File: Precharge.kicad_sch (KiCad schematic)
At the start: 27 parts, among them J1 SDC_OUT, J2 TSAL, J3 BMS, J4 SDC_IN, J5 CONN_ACC, J6 CONN_INV, J7 CONN_TSAL, K1 G2RG-2A-X DC12, K2 G2RL-1-E

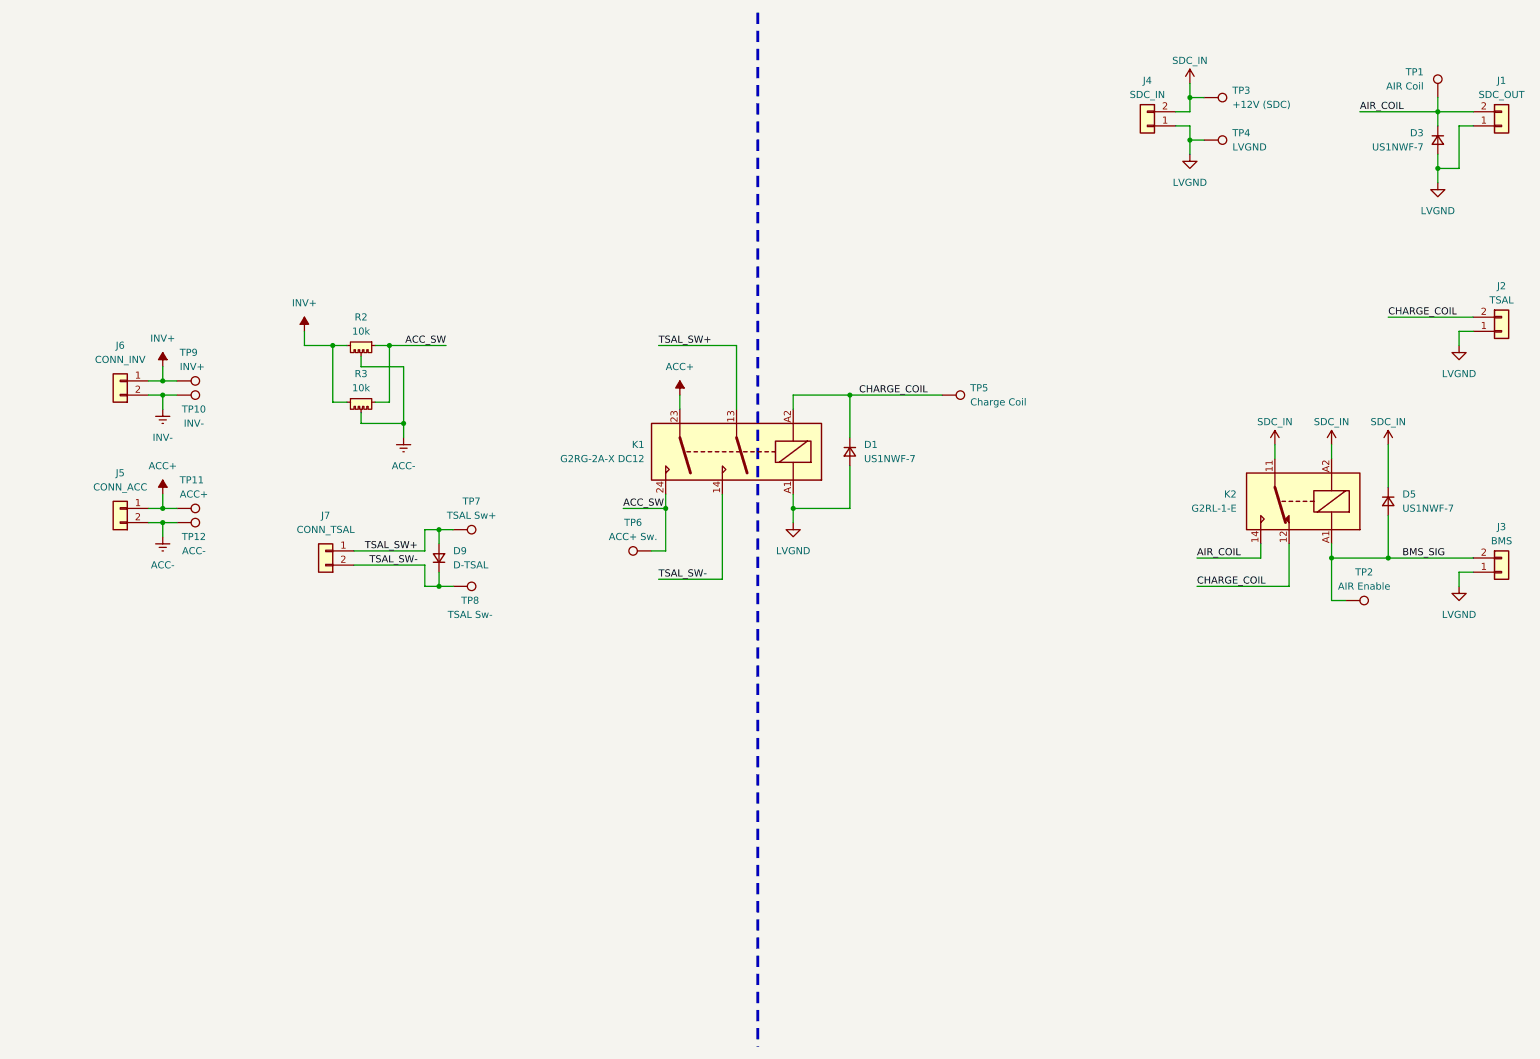
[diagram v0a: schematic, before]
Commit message: New schematic
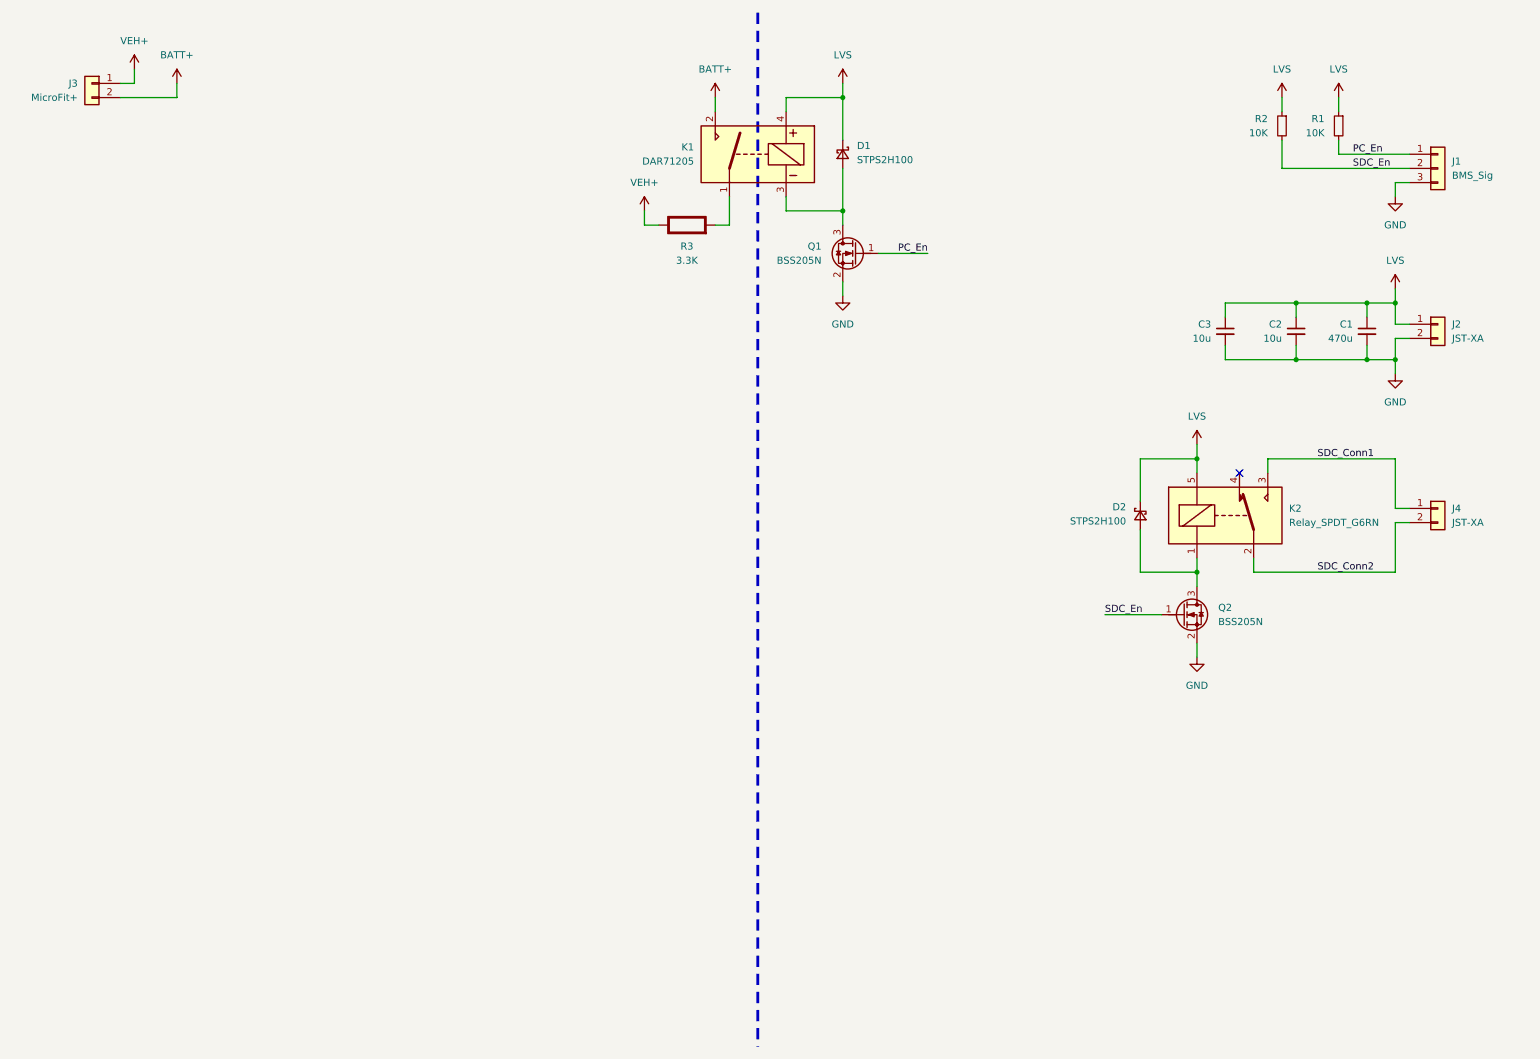
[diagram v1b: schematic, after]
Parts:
- removed D1, D3, D5: US1NWF-7, Diode_SMD:D_SOD-123F, symbol Device:D_Small
- removed D9: D-TSAL, Diode_SMD:D_SOD-123, symbol Device:D_Small
- removed J1: SDC_OUT, molexMiniFitJr:MFJ_2X1, symbol Connector_Generic:Conn_01x02
- removed J2: TSAL, molexMiniFitJr:MFJ_2X1, symbol Connector_Generic:Conn_01x02
- removed J3: BMS, molexMiniFitJr:MFJ_2X1, symbol Connector_Generic:Conn_01x02
- removed J4: SDC_IN, molexMiniFitJr:MFJ_2X1, symbol Connector_Generic:Conn_01x02
- removed J5: CONN_ACC, customFootprints:APP_ASMPR45-1X2-RK, symbol Connector_Generic:Conn_01x02
- removed J6: CONN_INV, customFootprints:APP_ASMPR45-1X2-RK, symbol Connector_Generic:Conn_01x02
- removed J7: CONN_TSAL, molexMiniFitJr:MFJ_2X1, symbol Connector_Generic:Conn_01x02
- removed K1: G2RG-2A-X DC12, Relay_THT:Relay_DPST_Omron_G2RL-2A, symbol Relay:G2RL-2A
- removed K2: G2RL-1-E, Relay_THT:Relay_SPDT_Omron_G2RL-1-E, symbol Relay:G2RL-1-E
- removed R2, R3: 10k, customFootprints:R_HS, symbol customSymbols:R_HS
- removed TP1: AIR Coil, TestPoint:TestPoint_Pad_D1.5mm, symbol Connector:TestPoint
- removed TP10: INV-, TestPoint:TestPoint_Pad_1.5x1.5mm, symbol Connector:TestPoint
- removed TP11: ACC+, TestPoint:TestPoint_Pad_D1.5mm, symbol Connector:TestPoint
- removed TP12: ACC-, TestPoint:TestPoint_Pad_1.5x1.5mm, symbol Connector:TestPoint
- removed TP2: AIR Enable, TestPoint:TestPoint_Pad_D1.5mm, symbol Connector:TestPoint
- removed TP3: +12V (SDC), TestPoint:TestPoint_Pad_1.5x1.5mm, symbol Connector:TestPoint
- removed TP4: LVGND, TestPoint:TestPoint_Pad_1.5x1.5mm, symbol Connector:TestPoint
- removed TP5: Charge Coil, TestPoint:TestPoint_Pad_D1.5mm, symbol Connector:TestPoint
- removed TP6: ACC+ Sw., TestPoint:TestPoint_Pad_D1.5mm, symbol Connector:TestPoint
- removed TP7: TSAL Sw+, TestPoint:TestPoint_Pad_D1.5mm, symbol Connector:TestPoint
- removed TP8: TSAL Sw-, TestPoint:TestPoint_Pad_D1.5mm, symbol Connector:TestPoint
- removed TP9: INV+, TestPoint:TestPoint_Pad_D1.5mm, symbol Connector:TestPoint
- added C1: 470u, Capacitor_SMD:CP_Elec_10x12.6, symbol Device:C_Small
- added C2, C3: 10u, Capacitor_SMD:C_1206_3216Metric_Pad1.33x1.80mm_HandSolder, symbol Device:C_Small
- added D1, D2: STPS2H100, Diode_SMD:D_SOD-123F, symbol Device:D_Schottky_Small
- added J1: BMS_Sig, Custom_MSM:Connector_JST-XA_3POS, symbol Custom_MSM:Connector_JST-XA_3POS
- added J2, J4: JST-XA, Custom_MSM:Connector_JST-XA_2POS, symbol Custom_MSM:Connector_JST-XA_2POS
- added J3: MicroFit+, Custom_MSM:Connector_MicroFit-Plus_2POS, symbol Custom_MSM.old:Connector_MicroFit-Plus_2POS
- added K1: DAR71205, Custom_MSM:Relay_HV, symbol Custom_MSM:Relay_NO_HV
- added K2: Relay_SPDT_G6RN, Custom_MSM:Relay_SPDT_G6RN, symbol Custom_MSM:Relay_SPDT_G6RN
- added Q1, Q2: BSS205N, Custom_MSM:MOSFET_Single_SOT-23, symbol Custom_MSM:MOSFET_N-CH
- added R1, R2: 10K, Resistor_SMD:R_0805_2012Metric_Pad1.20x1.40mm_HandSolder, symbol Device:R_Small
- added R3: 3.3K, customFootprints:HS100, symbol PCM_Elektuur:R
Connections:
- new net: K1.1, R3.2 (-)
- new net: D1.2 (A), K1.3, Q1.3 (D)
- new net: D2.2 (A), K2.1, Q2.3 (D)
- new net BATT+: J3.2 (Pin_2), K1.2
- new net GND: C1.2, C2.2, C3.2, J1.3 (Pin_3), J2.2 (Pin_2), Q1.2 (S), Q2.2 (S)
- new net LVS: C1.1, C2.1, C3.1, D1.1 (K), D2.1 (K), J2.1 (Pin_1), K1.4, K2.5, R1.1, R2.1
- new net PC_En: J1.1 (Pin_1), Q1.1 (G), R1.2
- new net SDC_Conn1: J4.1 (Pin_1), K2.3
- new net SDC_Conn2: J4.2 (Pin_2), K2.2
- new net SDC_En: J1.2 (Pin_2), Q2.1 (G), R2.2
- new net VEH+: J3.1 (Pin_1), R3.1 (+)
- no-connect marks 0 -> 1

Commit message: Finished schematic and PCB
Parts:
- removed C3: 10u, Capacitor_SMD:C_1206_3216Metric_Pad1.33x1.80mm_HandSolder, symbol Device:C_Small
- removed R1, R2: 10K, Resistor_SMD:R_0805_2012Metric_Pad1.20x1.40mm_HandSolder, symbol Device:R_Small
- removed R3: 3.3K, customFootprints:HS100, symbol PCM_Elektuur:R
- added C1: 10u, Capacitor_SMD:C_1206_3216Metric_Pad1.33x1.80mm_HandSolder, symbol Device:C_Small
- added R1, R2, R3, R4: 5K, Package_TO_SOT_SMD:TO-263-2, symbol customSymbols:R_HS
- added R10, R15, R18, R7: 97.6K, Resistor_SMD:R_0805_2012Metric_Pad1.20x1.40mm_HandSolder, symbol Device:R_Small
- added R11, R12, R16, R17, R19, R20, R8, R9: 105K, Resistor_SMD:R_0805_2012Metric_Pad1.20x1.40mm_HandSolder, symbol Device:R_Small
- added R13, R5: 20K, Resistor_SMD:R_0805_2012Metric_Pad1.20x1.40mm_HandSolder, symbol Device:R_Small
- added R14, R6: 10K, Resistor_SMD:R_0805_2012Metric_Pad1.20x1.40mm_HandSolder, symbol Device:R_Small
- added U1, U2: TLV1702, Custom_MSM:Comparator_Dual_VSSOP-8, symbol Custom_MSM:Comparator_Dual_Open-Coll
- J2: renamed from J4; value JST-XA -> SDC_IO
- J4: renamed from J2; value JST-XA -> LVS; S1PC (none) -> 0.30; S2PC (none) -> 0.36
- renumbered C1 to C3, J3 to J1, J1 to J3
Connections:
- net GND: now also C1.2, R10.2, R12.2, R14.2, R16.2, R18.2, R20.2, R6.2, R8.2, U1.4 (V-), U2.4 (V-)
- net LVS: now also C1.1, R13.1, R15.1, R17.1, R5.1, R7.1, R9.1, U1.8 (V+), U2.8 (V+)
- net PC_En: now also J3.2 (Pin_2), R19.1; no longer J3.1 (Pin_1), Q1.1 (G)
- net SDC_En: now also J3.1 (Pin_1), R11.1; no longer J3.2 (Pin_2), Q2.1 (G)
- net VEH+: now also R1.1, R1.2, R2.1, R2.2, R3.2, R4.2
- net at K1.1: now also R3.3, R4.3
- net SDC_Conn1 renamed SDC_1
- net SDC_Conn2 renamed SDC_2
- new net: R11.2, R12.1, U1.2 (-), U1.5 (+)
- new net: R1.3, R3.1
- new net: R17.2, R18.1, U2.6 (-)
- new net: R10.1, R9.2, U1.6 (-)
- new net: R19.2, R20.1, U2.2 (-), U2.5 (+)
- new net: R15.2, R16.1, U2.3 (+)
- new net: R7.2, R8.1, U1.3 (+)
- new net: R2.3, R4.1
- new net PC_Gate: Q1.1 (G), R13.2, R14.1, U2.1, U2.7
- new net SDC_Gate: Q2.1 (G), R5.2, R6.1, U1.1, U1.7
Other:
- note added: "BMS Signals"
- note added: "HV Input"
- note added: "IC Power"
- note added: "LVS Input"
- note added: "Precharge"
- note added: "Precharge SCS"
- note added: "SDC IO"
- note added: "SDC SCS"
- note added: "SDC Switching"
- moved on the sheet: C3, D1, D2, J1, J2, J3, J4, K1, K2, Q1, Q2

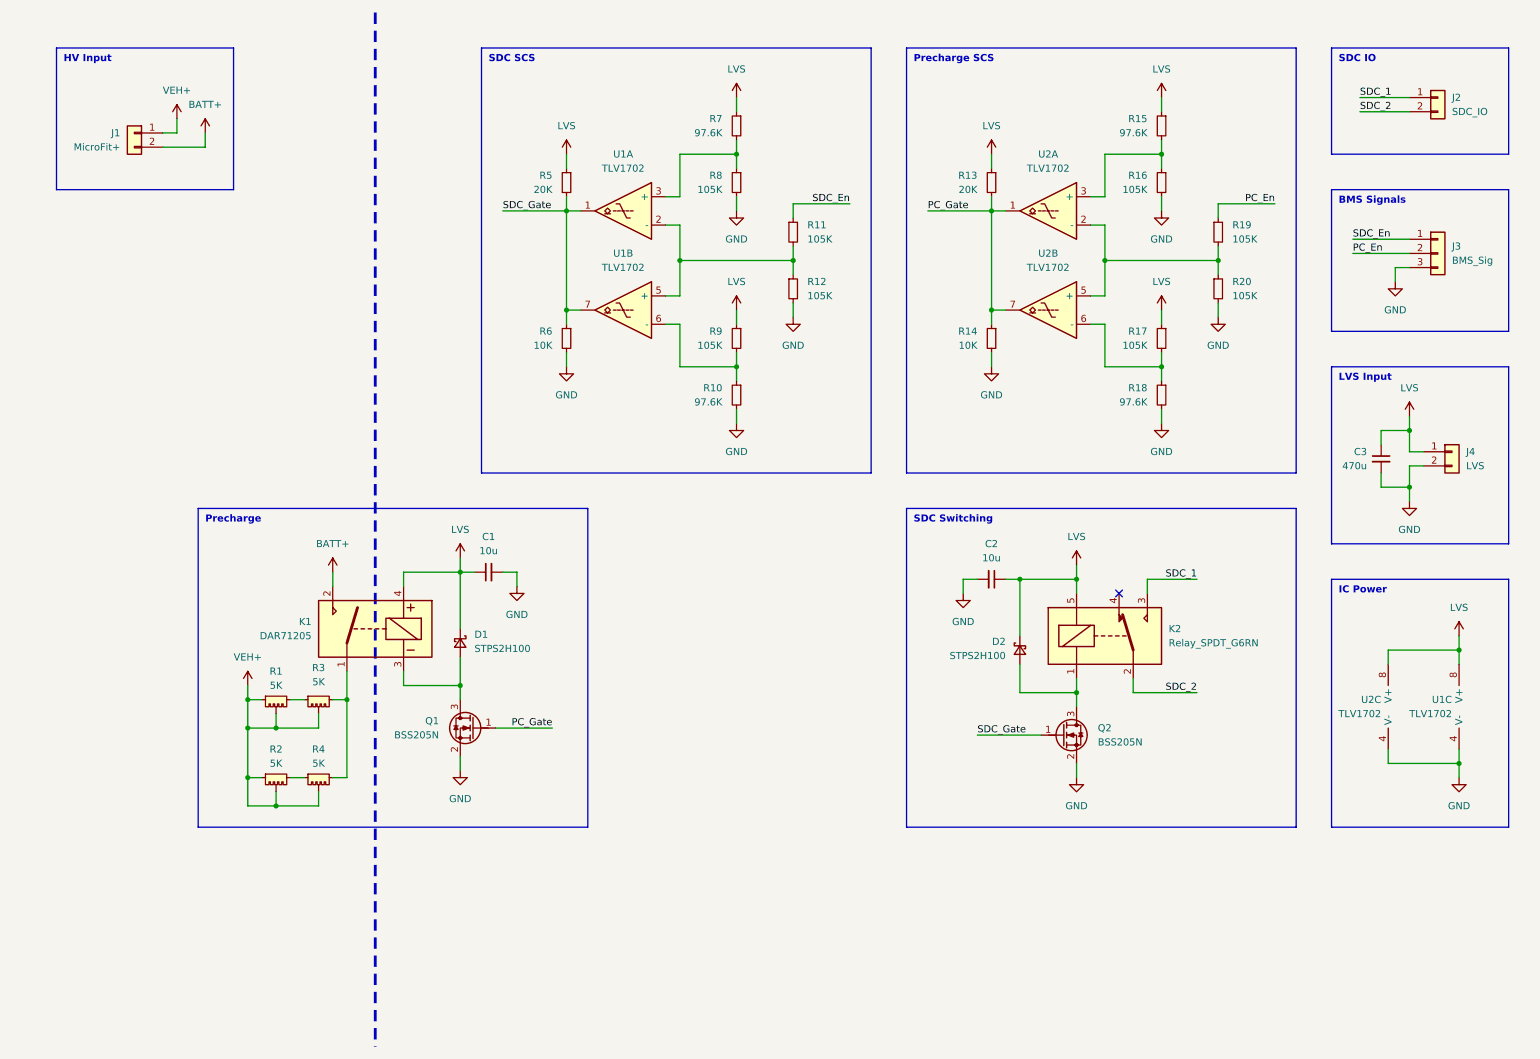
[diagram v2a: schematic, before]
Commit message: Downsized to extra small
New relay, longer precharge time, option to shorten and add parallel resistors for lower load
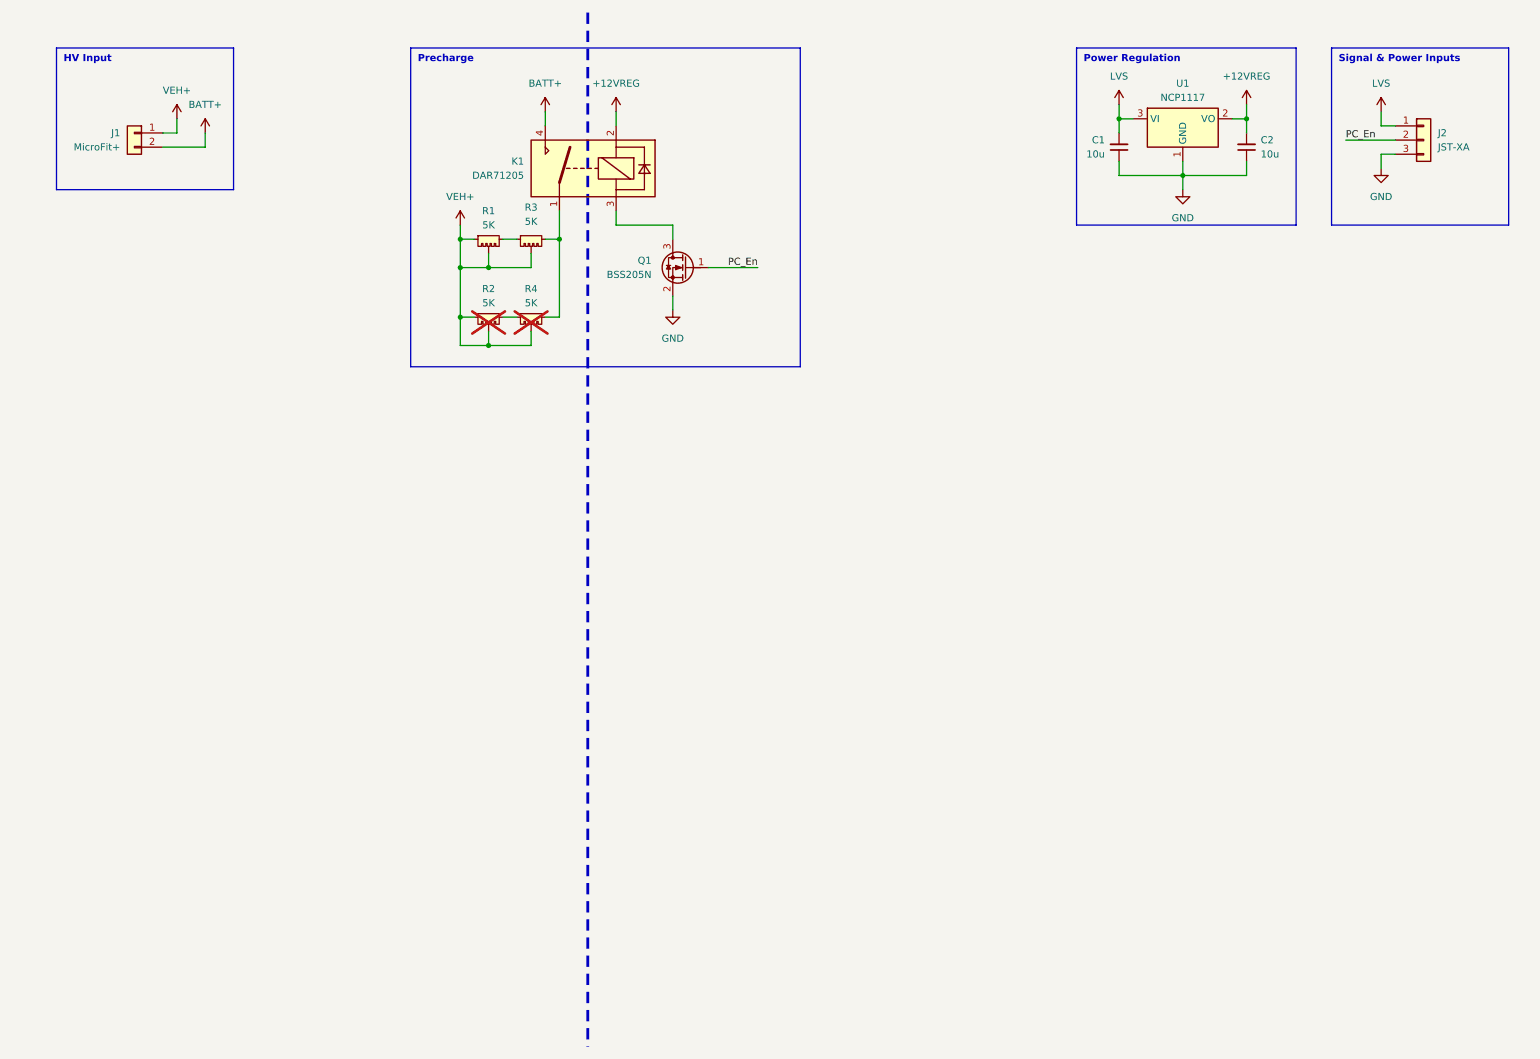
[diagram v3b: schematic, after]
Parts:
- removed C3: 470u, Capacitor_SMD:CP_Elec_10x12.6, symbol Device:C_Small
- removed D1, D2: STPS2H100, Diode_SMD:D_SOD-123F, symbol Device:D_Schottky_Small
- removed J2: SDC_IO, Custom_MSM:Connector_JST-XA_2POS, symbol Custom_MSM:Connector_JST-XA_2POS
- removed J3: BMS_Sig, Custom_MSM:Connector_JST-XA_3POS, symbol Custom_MSM:Connector_JST-XA_3POS
- removed J4: LVS, Custom_MSM:Connector_JST-XA_2POS, symbol Custom_MSM:Connector_JST-XA_2POS
- removed K2: Relay_SPDT_G6RN, Custom_MSM:Relay_SPDT_G6RN, symbol Custom_MSM:Relay_SPDT_G6RN
- removed Q2: BSS205N, Custom_MSM:MOSFET_Single_SOT-23, symbol Custom_MSM:MOSFET_N-CH
- removed R10, R15, R18, R7: 97.6K, Resistor_SMD:R_0805_2012Metric_Pad1.20x1.40mm_HandSolder, symbol Device:R_Small
- removed R11, R12, R16, R17, R19, R20, R8, R9: 105K, Resistor_SMD:R_0805_2012Metric_Pad1.20x1.40mm_HandSolder, symbol Device:R_Small
- removed R13, R5: 20K, Resistor_SMD:R_0805_2012Metric_Pad1.20x1.40mm_HandSolder, symbol Device:R_Small
- removed R14, R6: 10K, Resistor_SMD:R_0805_2012Metric_Pad1.20x1.40mm_HandSolder, symbol Device:R_Small
- removed U1, U2: TLV1702, Custom_MSM:Comparator_Dual_VSSOP-8, symbol Custom_MSM:Comparator_Dual_Open-Coll
- added J2: JST-XA, Library:Connector_JST-XA_3POS, symbol Custom_MSM:Connector_JST-XA_3POS
- added U1: NCP1117, Library:Regulator_Linear_SOT-223-4, symbol Custom_MSM:Regulator_Linear_12V
- C1, C2: footprint Capacitor_SMD:C_1206_3216Metric_Pad1.33x1.80mm_HandSolder -> Library:C_1206_3216Metric_Pad1.33x1.80mm_HandSolder; KiLib_Generator (none) -> SMD_2terminal_chip_molded
- J1: footprint Custom_MSM:Connector_MicroFit-Plus_2POS -> Library:Connector_MicroFit-Plus_2POS
- K1: footprint Custom_MSM:Relay_HV -> Library:Relay_HV
- Q1: footprint Custom_MSM:MOSFET_Single_SOT-23 -> Library:MOSFET_Single_SOT-23
- R1, R3: footprint Package_TO_SOT_SMD:TO-263-2 -> Library:TO-263-2; KiLib_Generator (none) -> package/TO_SOT/SMD
- R2, R4: now not fitted
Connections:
- net PC_Gate is gone; now on net PC_En: Q1.1 (G)
- net BATT+: now also K1.4; no longer K1.2
- net GND: now also C1.1, C2.1, J2.3 (Pin_3), U1.1 (GND); no longer C1.2, C2.2
- net LVS: now also C1.2, J2.1 (Pin_1), U1.3 (VI); no longer C1.1, C2.1, K1.4
- net PC_En: now also J2.2 (Pin_2)
- new net +12VREG: C2.2, K1.2, U1.2 (VO), U1.4 (TAB)
- no-connect marks 1 -> 0
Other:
- note added: "Power Regulation"
- note added: "Signal & Power Inputs"
- note removed: "BMS Signals"
- note removed: "IC Power"
- note removed: "LVS Input"
- note removed: "Precharge SCS"
- note removed: "SDC IO"
- note removed: "SDC SCS"
- note removed: "SDC Switching"
- moved on the sheet: Q1, R1, R3
